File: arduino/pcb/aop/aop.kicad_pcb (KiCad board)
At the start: 2 copper layers, 45 x 55 mm, 14 parts, among them J1 Conn_01x02_Pin, Q1 AO4435, SW1 SW_Push, SW2 SW_Push, U1 ESP32-C3_SUPERMINI_TH

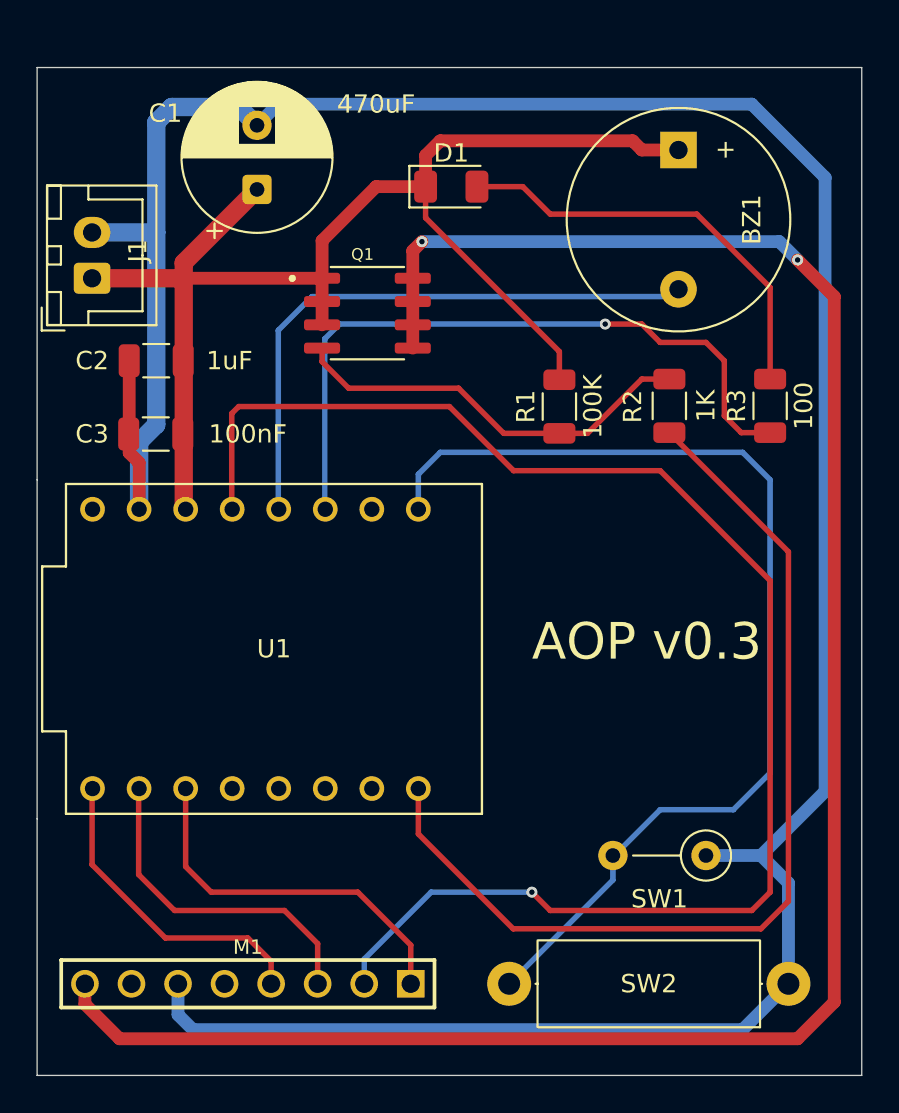
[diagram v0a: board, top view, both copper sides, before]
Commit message: [pcb] Add DS3231
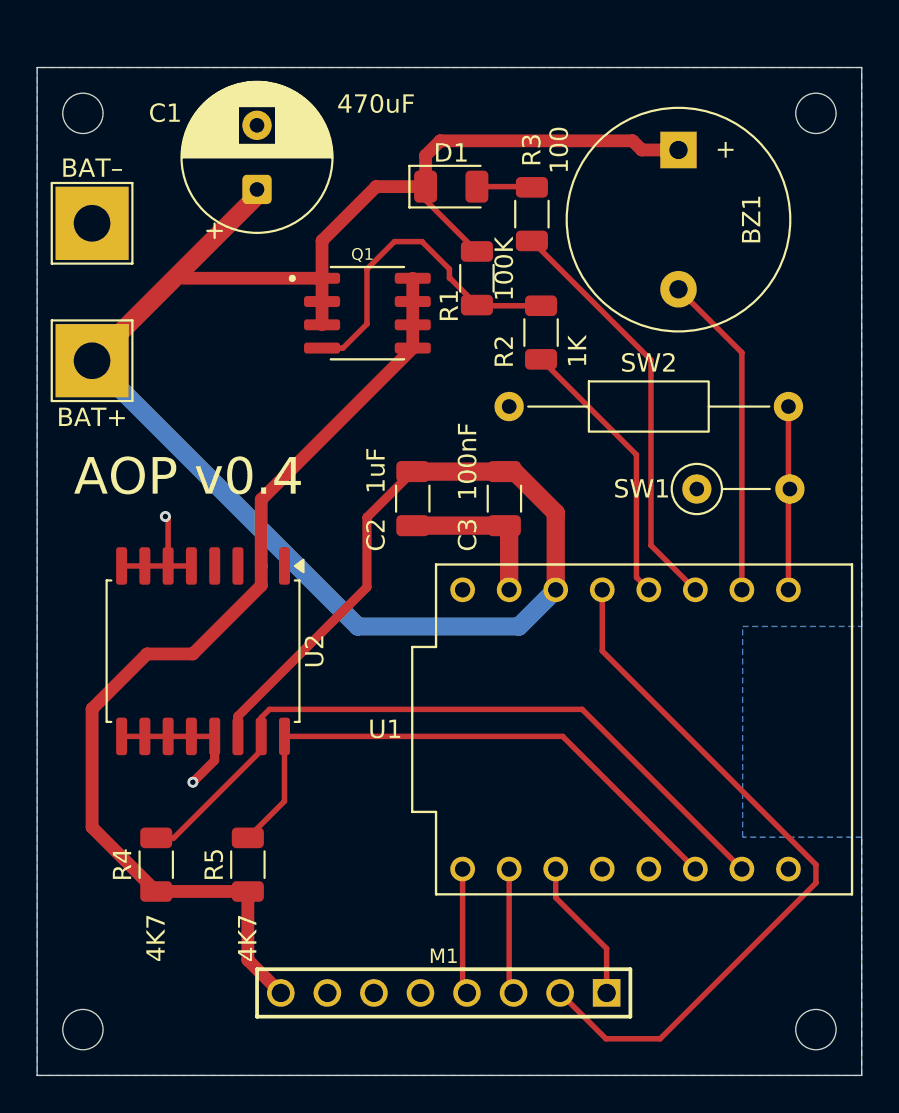
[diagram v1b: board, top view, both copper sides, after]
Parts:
- removed J1: Conn_01x02_Pin, Connector_JST:JST_XH_B2B-XH-A_1x02_P2.50mm_Vertical
- added H1: MountingHole, MountingHole:MountingHole_2.2mm_M2, F.Cu at (128.5, 83.0)
- added H2: MountingHole, MountingHole:MountingHole_2.2mm_M2, F.Cu at (168.5, 83.0)
- added H3: MountingHole, MountingHole:MountingHole_2.2mm_M2, F.Cu at (128.5, 133.0)
- added H4: MountingHole, MountingHole:MountingHole_2.2mm_M2, F.Cu at (168.5, 133.0)
- added R4: 4K7, Resistor_SMD:R_1206_3216Metric, F.Cu at (132.5, 124.0)
- added R5: 4K7, Resistor_SMD:R_1206_3216Metric, F.Cu at (137.5, 124.0)
- added TP1: BAT+, TestPoint:TestPoint_THTPad_4.0x4.0mm_Drill2.0mm, F.Cu at (129.0, 96.5)
- added TP2: BAT–, TestPoint:TestPoint_THTPad_4.0x4.0mm_Drill2.0mm, F.Cu at (129.0, 89.0)
- added U2: DS3231M, Package_SO:SOIC-16W_7.5x10.3mm_P1.27mm, F.Cu at (135.1, 112.3)
- SW2: footprint Resistor_THT:R_Axial_DIN0414_L11.9mm_D4.5mm_P15.24mm_Horizontal -> Resistor_THT:R_Axial_DIN0207_L6.3mm_D2.5mm_P15.24mm_Horizontal
- moved SW2 35.0 mm to (151.8, 99.0), turned to 0 degrees
- moved U1 20.7 mm to (159.1, 116.6)
- moved SW1 20.0 mm to (162.0, 103.5), turned to 0 degrees
- moved C3 19.3 mm to (151.5, 104.0), turned to -90 degrees
- moved R3 16.7 mm to (153.0, 88.5)
- moved C2 15.9 mm to (146.5, 104.0), turned to -90 degrees
- moved M1 10.7 mm to (148.2, 131.0)
- moved R1 8.32 mm to (150.0, 92.0)
- moved R2 8.06 mm to (153.5, 95.0)
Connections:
- R2 pad 2: Net-(U1-GPIO21) -> Net-(U1-GPIO3)
- U1 pad 1: unconnected-(U1-GPIO1-Pad1) -> Net-(BZ1--)
- U1 pad 10: unconnected-(U1-GPIO10-Pad10) -> Net-(U1-GPIO10)
- U1 pad 20: unconnected-(U1-GPIO20-Pad20) -> Net-(U1-GPIO20)
- U1 pad 21: Net-(U1-GPIO21) -> unconnected-(U1-GPIO21-Pad21)
- U1 pad 3: Net-(BZ1--) -> Net-(U1-GPIO3)
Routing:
- net GND: track 158.2 -> 23.3 mm, vias 0 -> 2
- net +3.3VA: track 111.9 -> 54.9 mm, vias 2 -> 0
- net Net-(U1-GPIO21): track 53.7 -> 0.00 mm
- net Net-(U1-GPIO0): track 58.0 -> 10.0 mm
- net +BATT: track 72.8 -> 116.3 mm
- net Net-(M1-SCK): track 81.5 -> 39.3 mm, vias 1 -> 0
- net Net-(U1-GPIO20): track 0.00 -> 39.5 mm
- net Net-(U1-GPIO10): track 0.00 -> 31.8 mm
- net Net-(D1-A): track 23.3 -> 2.50 mm
- net Net-(U1-GPIO2): track 38.2 -> 22.7 mm, vias 1 -> 0
- net Net-(U1-GPIO3): track 0.00 -> 15.0 mm
- net Net-(BZ1--): track 32.5 -> 17.8 mm
- net Net-(M1-SDA): track 20.4 -> 7.51 mm
- net Net-(M1-MOSI): track 18.2 -> 6.86 mm
- net Net-(M1-MISO): track 17.3 -> 6.86 mm
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- added copper zone on B.Cu, net GND
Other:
- outline, holes or cut-outs redrawn

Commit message: [pcb] Choose closer pins for SPI
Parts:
- C1: value 470uF -> 470 uF
- C2: value 1uF -> 1 uF
- C3: value 100nF -> 100 nF
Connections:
- U1 pad 4: Net-(M1-SCK) -> unconnected-(U1-GPIO4-Pad4)
- U1 pad 7: Net-(M1-SDA) -> Net-(M1-SCK)
- U1 pad 8: unconnected-(U1-GPIO8-Pad8) -> Net-(M1-SDA)
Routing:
- net Net-(M1-SCK): track 39.3 -> 6.86 mm
- net Net-(M1-SDA): track 7.51 -> 6.86 mm
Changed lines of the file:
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@@
 		(capping no)
 		(filling no)
-		(zone_defaults)
 		(pcbplotparams
 			(layerselection 0x00000000_00000000_55555555_5755f5ff)
@@
 			)
 		)
-		(property "Value" "100nF"
+		(property "Value" "100 nF"
 			(at -2.025 2 90)
 			(layer "F.SilkS")
@@
 			)
 		)
-		(property "Value" "470uF"
+		(property "Value" "470 uF"
 			(at 4.652651 6.5 180)
 			(layer "F.SilkS")
@@
 			)
 		)
-		(property "Value" "1uF"
+		(property "Value" "1 uF"
 			(at -1.525 2 90)
 			(layer "F.SilkS")
@@
 			(layers "*.Cu" "*.Mask")
 			(remove_unused_layers no)
-			(net "Net-(M1-SCK)")
+			(net "unconnected-(U1-GPIO4-Pad4)")
 			(pinfunction "GPIO4_4")
 			(pintype "bidirectional")
@@
 			(layers "*.Cu" "*.Mask")
 			(remove_unused_layers no)
-			(net "Net-(M1-SDA)")
+			(net "Net-(M1-SCK)")
 			(pinfunction "GPIO7_7")
 			(pintype "bidirectional")
@@
 			(layers "*.Cu" "*.Mask")
 			(remove_unused_layers no)
-			(net "unconnected-(U1-GPIO8-Pad8)")
+			(net "Net-(M1-SDA)")
 			(pinfunction "GPIO8_8")
 			(pintype "bidirectional")
@@
 	)
 	(segment
-		(start 154.3 125.8)
-		(end 157.08 128.58)
+		(start 157.08 131)
+		(end 157.08 124.48)
 		(width 0.3)
 		(layer "F.Cu")
@@
 	)
 	(segment
-		(start 157.08 128.58)
-		(end 157.08 131)
+		(start 157.08 124.48)
+		(end 156.84 124.24)
 		(width 0.3)
 		(layer "F.Cu")
@@
 	)
 	(segment
-		(start 154.3 124.64)
-		(end 154.3 125.8)
-		(width 0.3)
-		(layer "F.Cu")
-		(net "Net-(M1-SDA)")
-	)
-	(segment
-		(start 160 133.5)
-		(end 157.04 133.5)
-		(width 0.3)
-		(layer "F.Cu")
-		(net "Net-(M1-SCK)")
-	)
-	(segment
-		(start 168.5 125)
-		(end 160 133.5)
-		(width 0.3)
-		(layer "F.Cu")
-		(net "Net-(M1-SCK)")
-	)
-	(segment
-		(start 168.5 124)
-		(end 168.5 125)
-		(width 0.3)
-		(layer "F.Cu")
-		(net "Net-(M1-SCK)")
-	)
-	(segment
-		(start 156.84 112.34)
-		(end 168.5 124)
-		(width 0.3)
-		(layer "F.Cu")
-		(net "Net-(M1-SCK)")
-	)
-	(segment
-		(start 157.04 133.5)
-		(end 154.54 131)
+		(start 154.54 124.48)
+		(end 154.3 124.24)
 		(width 0.3)
 		(layer "F.Cu")
@@
 	)
 	(segment
-		(start 156.84 109)
-		(end 156.84 112.34)
+		(start 154.54 131)
+		(end 154.54 124.48)
 		(width 0.3)
 		(layer "F.Cu")

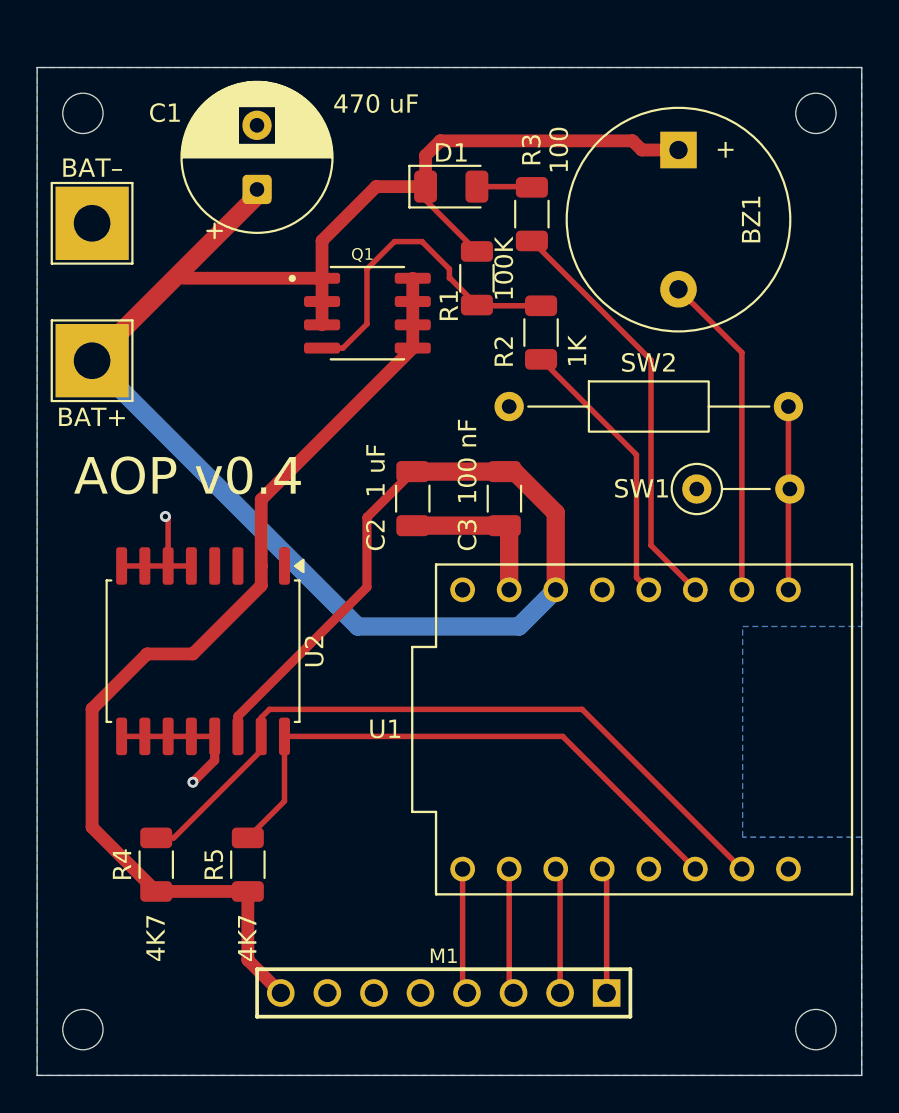
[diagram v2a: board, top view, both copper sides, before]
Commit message: [pcb] Reroute to improve ground plane continuity
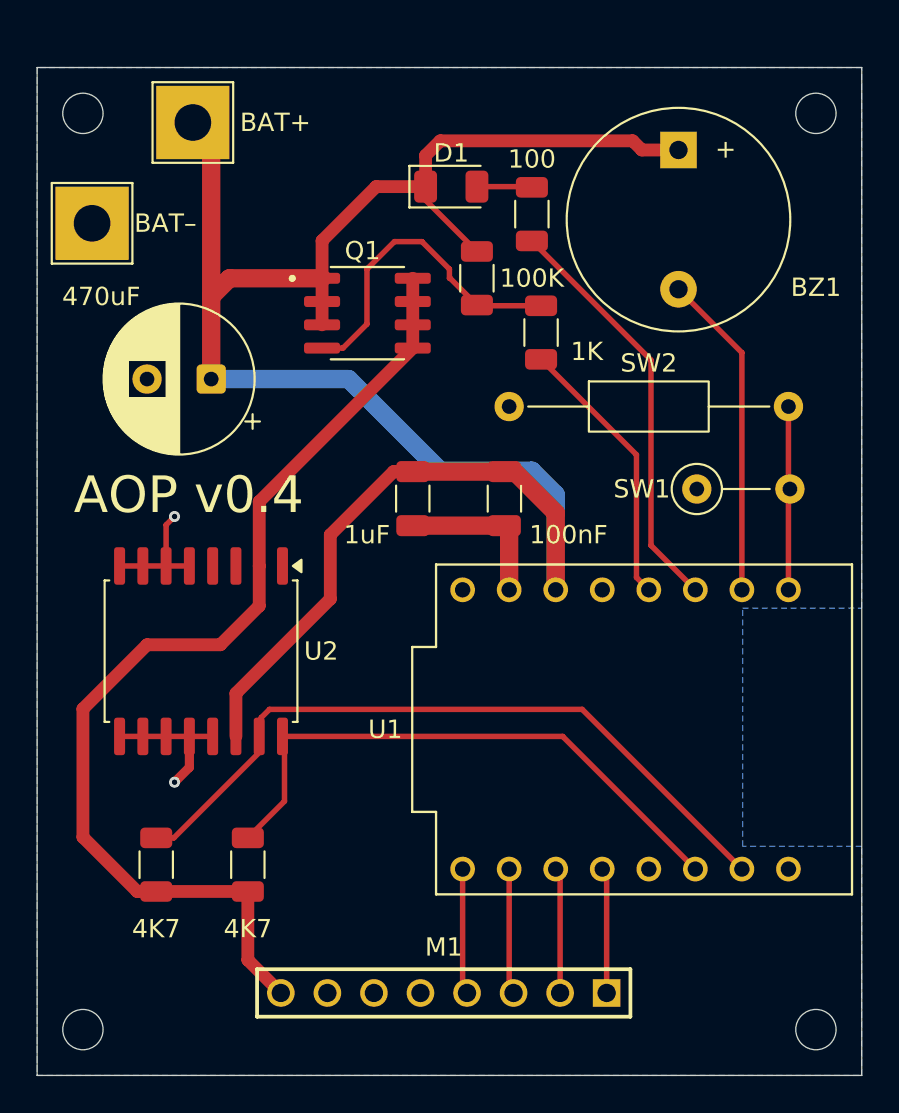
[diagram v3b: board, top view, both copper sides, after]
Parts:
- C1: value 470 uF -> 470uF
- C2: value 1 uF -> 1uF
- C3: value 100 nF -> 100nF
- moved TP1 14.1 mm to (134.5, 83.5)
- moved C1 10.6 mm to (135.5, 97.5), turned to 180 degrees
- moved U2 0.11 mm to (134.9, 112.3)
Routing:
- net +BATT: track 116.3 -> 111.2 mm
- net +3.3VA: track 54.9 -> 56.8 mm

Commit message: [pcb] Send v0.4 for fabrication
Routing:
- added copper zone on F.Cu, net GND
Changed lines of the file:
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@@
 	(zone
 		(net "GND")
-		(layer "B.Cu")
+		(layers "F.Cu" "B.Cu")
 		(hatch edge 0.5)
 		(connect_pads
